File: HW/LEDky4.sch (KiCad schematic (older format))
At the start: 8 parts

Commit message: add some codes for JLCPCB, change package and schematic of CP2102
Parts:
- C? (x4): LCSC (none) -> C1525
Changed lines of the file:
@@
 F 2 "Capacitor_SMD:C_0402_1005Metric" H 2738 1450 50  0001 C CNN
 F 3 "~" H 2700 1600 50  0001 C CNN
+F 4 "C1525" H 2700 1600 50  0001 C CNN "LCSC"
 	1    2700 1600
 	1    0    0    -1
@@
 F 2 "Capacitor_SMD:C_0402_1005Metric" H 4138 1450 50  0001 C CNN
 F 3 "~" H 4100 1600 50  0001 C CNN
+F 4 "C1525" H 4100 1600 50  0001 C CNN "LCSC"
 	1    4100 1600
 	1    0    0    -1
@@
 F 2 "Capacitor_SMD:C_0402_1005Metric" H 5438 1450 50  0001 C CNN
 F 3 "~" H 5400 1600 50  0001 C CNN
+F 4 "C1525" H 5400 1600 50  0001 C CNN "LCSC"
 	1    5400 1600
 	1    0    0    -1
@@
 F 2 "Capacitor_SMD:C_0402_1005Metric" H 6838 1450 50  0001 C CNN
 F 3 "~" H 6800 1600 50  0001 C CNN
+F 4 "C1525" H 6800 1600 50  0001 C CNN "LCSC"
 	1    6800 1600
 	1    0    0    -1
@@
 F 2 "Capacitor_SMD:C_0402_1005Metric" H 2738 1450 50  0001 C CNN
 F 3 "~" H 2700 1600 50  0001 C CNN
+F 4 "C1525" H 2700 1600 50  0001 C CNN "LCSC"
 	1    2700 1600
 	1    0    0    -1
@@
 F 2 "Capacitor_SMD:C_0402_1005Metric" H 4138 1450 50  0001 C CNN
 F 3 "~" H 4100 1600 50  0001 C CNN
+F 4 "C1525" H 4100 1600 50  0001 C CNN "LCSC"
 	1    4100 1600
 	1    0    0    -1
@@
 F 2 "Capacitor_SMD:C_0402_1005Metric" H 5438 1450 50  0001 C CNN
 F 3 "~" H 5400 1600 50  0001 C CNN
+F 4 "C1525" H 5400 1600 50  0001 C CNN "LCSC"
 	1    5400 1600
 	1    0    0    -1
@@
 F 2 "Capacitor_SMD:C_0402_1005Metric" H 6838 1450 50  0001 C CNN
 F 3 "~" H 6800 1600 50  0001 C CNN
+F 4 "C1525" H 6800 1600 50  0001 C CNN "LCSC"
 	1    6800 1600
 	1    0    0    -1

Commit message: add some codes for JLCPCB
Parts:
- D? (x4): LCSC (none) -> C114587
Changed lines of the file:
@@
 F 2 "LED_SMD:LED_WS2812B_PLCC4_5.0x5.0mm_P3.2mm" H 2200 1500 50  0001 L TNN
 F 3 "https://cdn-shop.adafruit.com/datasheets/WS2812B.pdf" H 2250 1425 50  0001 L TNN
+F 4 "C114587" H 2150 1800 50  0001 C CNN "LCSC"
 	1    2150 1800
 	1    0    0    -1
@@
 F 2 "LED_SMD:LED_WS2812B_PLCC4_5.0x5.0mm_P3.2mm" H 3600 1500 50  0001 L TNN
 F 3 "https://cdn-shop.adafruit.com/datasheets/WS2812B.pdf" H 3650 1425 50  0001 L TNN
+F 4 "C114587" H 3550 1800 50  0001 C CNN "LCSC"
 	1    3550 1800
 	1    0    0    -1
@@
 F 2 "LED_SMD:LED_WS2812B_PLCC4_5.0x5.0mm_P3.2mm" H 4900 1500 50  0001 L TNN
 F 3 "https://cdn-shop.adafruit.com/datasheets/WS2812B.pdf" H 4950 1425 50  0001 L TNN
+F 4 "C114587" H 4850 1800 50  0001 C CNN "LCSC"
 	1    4850 1800
 	1    0    0    -1
@@
 F 2 "LED_SMD:LED_WS2812B_PLCC4_5.0x5.0mm_P3.2mm" H 6300 1500 50  0001 L TNN
 F 3 "https://cdn-shop.adafruit.com/datasheets/WS2812B.pdf" H 6350 1425 50  0001 L TNN
+F 4 "C114587" H 6250 1800 50  0001 C CNN "LCSC"
 	1    6250 1800
 	1    0    0    -1
@@
 F 2 "LED_SMD:LED_WS2812B_PLCC4_5.0x5.0mm_P3.2mm" H 2200 1500 50  0001 L TNN
 F 3 "https://cdn-shop.adafruit.com/datasheets/WS2812B.pdf" H 2250 1425 50  0001 L TNN
+F 4 "C114587" H 2150 1800 50  0001 C CNN "LCSC"
 	1    2150 1800
 	1    0    0    -1
@@
 F 2 "LED_SMD:LED_WS2812B_PLCC4_5.0x5.0mm_P3.2mm" H 3600 1500 50  0001 L TNN
 F 3 "https://cdn-shop.adafruit.com/datasheets/WS2812B.pdf" H 3650 1425 50  0001 L TNN
+F 4 "C114587" H 3550 1800 50  0001 C CNN "LCSC"
 	1    3550 1800
 	1    0    0    -1
@@
 F 2 "LED_SMD:LED_WS2812B_PLCC4_5.0x5.0mm_P3.2mm" H 4900 1500 50  0001 L TNN
 F 3 "https://cdn-shop.adafruit.com/datasheets/WS2812B.pdf" H 4950 1425 50  0001 L TNN
+F 4 "C114587" H 4850 1800 50  0001 C CNN "LCSC"
 	1    4850 1800
 	1    0    0    -1
@@
 F 2 "LED_SMD:LED_WS2812B_PLCC4_5.0x5.0mm_P3.2mm" H 6300 1500 50  0001 L TNN
 F 3 "https://cdn-shop.adafruit.com/datasheets/WS2812B.pdf" H 6350 1425 50  0001 L TNN
+F 4 "C114587" H 6250 1800 50  0001 C CNN "LCSC"
 	1    6250 1800
 	1    0    0    -1

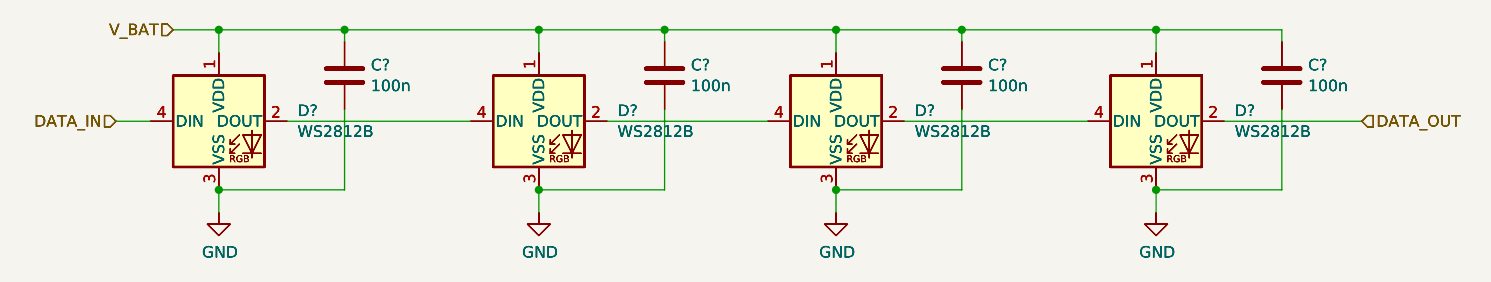
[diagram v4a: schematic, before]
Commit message: numbering components, place components on board
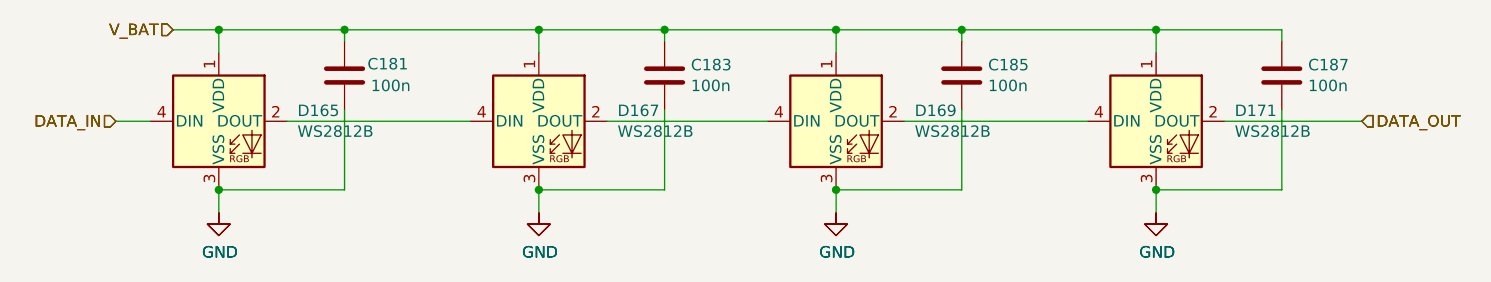
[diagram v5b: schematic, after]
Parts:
- removed C? (x4): 100n, Capacitor_SMD:C_0402_1005Metric, symbol Device:C
- removed D? (x4): WS2812B, LED_SMD:LED_WS2812B_PLCC4_5.0x5.0mm_P3.2mm, symbol LED:WS2812B
- added C117, C119, C121, C123: 100n, Capacitor_SMD:C_0402_1005Metric, symbol Device:C
- added D101, D103, D105, D107: WS2812B, LED_SMD:LED_WS2812B_PLCC4_5.0x5.0mm_P3.2mm, symbol LED:WS2812B
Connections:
- net DATA_IN: now also D101.4 (DIN)
- net DATA_OUT: now also D107.2 (DOUT)
- net GND: now also C117.2, C119.2, C121.2, C123.2, D101.3 (VSS), D103.3 (VSS), D105.3 (VSS), D107.3 (VSS)
- net V_BAT: now also C117.1, C119.1, C121.1, C123.1, D101.1 (VDD), D103.1 (VDD), D105.1 (VDD), D107.1 (VDD)
- new net: D101.2 (DOUT), D103.4 (DIN)
- new net: D103.2 (DOUT), D105.4 (DIN)
- new net: D105.2 (DOUT), D107.4 (DIN)

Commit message: repair package of TP4056
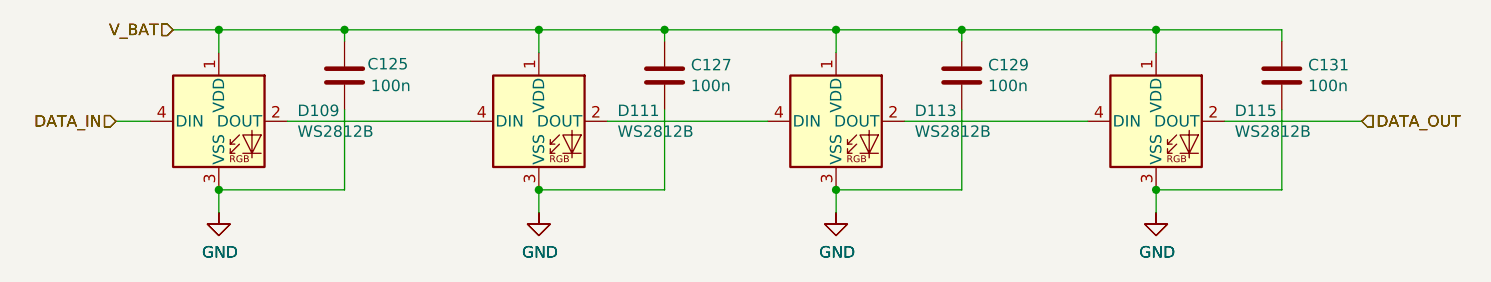
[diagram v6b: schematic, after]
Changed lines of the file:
@@
 $Descr A4 11693 8268
 encoding utf-8
-Sheet 42 44
+Sheet 35 44
 Title ""
 Date ""
@@
 AR Path="/5F79BCD0/5F79846B/5F78FD5C" Ref="#PWR0218"  Part="1"
 AR Path="/5F79BCD0/5F798482/5F78FD5C" Ref="#PWR0226"  Part="1"
-F 0 "#PWR0306" H 2150 1950 50  0001 C CNN
+F 0 "#PWR0250" H 2150 1950 50  0001 C CNN
 F 1 "GND" H 2155 2027 50  0000 C CNN
 F 2 "" H 2150 2200 50  0001 C CNN
@@
 AR Path="/5F79BCD0/5F79846B/5F78FD62" Ref="C93"  Part="1"
 AR Path="/5F79BCD0/5F798482/5F78FD62" Ref="C101"  Part="1"
-F 0 "C181" H 2800 1650 50  0000 L CNN
+F 0 "C125" H 2800 1650 50  0000 L CNN
 F 1 "100n" H 2815 1555 50  0000 L CNN
 F 2 "Capacitor_SMD:C_0402_1005Metric" H 2738 1450 50  0001 C CNN
@@
 AR Path="/5F79BCD0/5F79846B/5F78FD71" Ref="D79"  Part="1"
 AR Path="/5F79BCD0/5F798482/5F78FD71" Ref="D87"  Part="1"
-F 0 "D167" H 3894 1846 50  0000 L CNN
+F 0 "D111" H 3894 1846 50  0000 L CNN
 F 1 "WS2812B" H 3894 1755 50  0000 L CNN
 F 2 "LED_SMD:LED_WS2812B_PLCC4_5.0x5.0mm_P3.2mm" H 3600 1500 50  0001 L TNN
@@
 AR Path="/5F79BCD0/5F79846B/5F798BEB" Ref="#PWR0219"  Part="1"
 AR Path="/5F79BCD0/5F798482/5F798BEB" Ref="#PWR0227"  Part="1"
-F 0 "#PWR0307" H 3550 1950 50  0001 C CNN
+F 0 "#PWR0251" H 3550 1950 50  0001 C CNN
 F 1 "GND" H 3555 2027 50  0000 C CNN
 F 2 "" H 3550 2200 50  0001 C CNN
@@
 AR Path="/5F79BCD0/5F79846B/5F798BEE" Ref="#PWR0220"  Part="1"
 AR Path="/5F79BCD0/5F798482/5F798BEE" Ref="#PWR0228"  Part="1"
-F 0 "#PWR0308" H 4850 1950 50  0001 C CNN
+F 0 "#PWR0252" H 4850 1950 50  0001 C CNN
 F 1 "GND" H 4855 2027 50  0000 C CNN
 F 2 "" H 4850 2200 50  0001 C CNN
@@
 AR Path="/5F79BCD0/5F79846B/5F78FDA5" Ref="D83"  Part="1"
 AR Path="/5F79BCD0/5F798482/5F78FDA5" Ref="D91"  Part="1"
-F 0 "D171" H 6594 1846 50  0000 L CNN
+F 0 "D115" H 6594 1846 50  0000 L CNN
 F 1 "WS2812B" H 6594 1755 50  0000 L CNN
 F 2 "LED_SMD:LED_WS2812B_PLCC4_5.0x5.0mm_P3.2mm" H 6300 1500 50  0001 L TNN
@@
 AR Path="/5F79BCD0/5F79846B/5F78FDAB" Ref="#PWR0221"  Part="1"
 AR Path="/5F79BCD0/5F798482/5F78FDAB" Ref="#PWR0229"  Part="1"
-F 0 "#PWR0309" H 6250 1950 50  0001 C CNN
+F 0 "#PWR0253" H 6250 1950 50  0001 C CNN
 F 1 "GND" H 6255 2027 50  0000 C CNN
 F 2 "" H 6250 2200 50  0001 C CNN
@@
 AR Path="/5F79BCD0/5F79846B/5F78FDB1" Ref="C99"  Part="1"
 AR Path="/5F79BCD0/5F798482/5F78FDB1" Ref="C107"  Part="1"
-F 0 "C187" H 6915 1646 50  0000 L CNN
+F 0 "C131" H 6915 1646 50  0000 L CNN
 F 1 "100n" H 6915 1555 50  0000 L CNN
 F 2 "Capacitor_SMD:C_0402_1005Metric" H 6838 1450 50  0001 C CNN
@@
 AR Path="/5F79BCD0/5F79846B/5F78FD56" Ref="D77"  Part="1"
 AR Path="/5F79BCD0/5F798482/5F78FD56" Ref="D85"  Part="1"
-F 0 "D165" H 2494 1846 50  0000 L CNN
+F 0 "D109" H 2494 1846 50  0000 L CNN
 F 1 "WS2812B" H 2494 1755 50  0000 L CNN
 F 2 "LED_SMD:LED_WS2812B_PLCC4_5.0x5.0mm_P3.2mm" H 2200 1500 50  0001 L TNN
@@
 AR Path="/5F79BCD0/5F79846B/5F798BE8" Ref="#PWR0222"  Part="1"
 AR Path="/5F79BCD0/5F798482/5F798BE8" Ref="#PWR0230"  Part="1"
-F 0 "#PWR0310" H 2150 1950 50  0001 C CNN
+F 0 "#PWR0254" H 2150 1950 50  0001 C CNN
 F 1 "GND" H 2155 2027 50  0000 C CNN
 F 2 "" H 2150 2200 50  0001 C CNN
@@
 AR Path="/5F79BCD0/5F79846B/5F78FD77" Ref="#PWR0223"  Part="1"
 AR Path="/5F79BCD0/5F798482/5F78FD77" Ref="#PWR0231"  Part="1"
-F 0 "#PWR0311" H 3550 1950 50  0001 C CNN
+F 0 "#PWR0255" H 3550 1950 50  0001 C CNN
 F 1 "GND" H 3555 2027 50  0000 C CNN
 F 2 "" H 3550 2200 50  0001 C CNN
@@
 AR Path="/5F79BCD0/5F79846B/5F78FD7D" Ref="C95"  Part="1"
 AR Path="/5F79BCD0/5F798482/5F78FD7D" Ref="C103"  Part="1"
-F 0 "C183" H 4215 1646 50  0000 L CNN
+F 0 "C127" H 4215 1646 50  0000 L CNN
 F 1 "100n" H 4215 1555 50  0000 L CNN
 F 2 "Capacitor_SMD:C_0402_1005Metric" H 4138 1450 50  0001 C CNN
@@
 AR Path="/5F79BCD0/5F79846B/5F78FD8B" Ref="D81"  Part="1"
 AR Path="/5F79BCD0/5F798482/5F78FD8B" Ref="D89"  Part="1"
-F 0 "D169" H 5194 1846 50  0000 L CNN
+F 0 "D113" H 5194 1846 50  0000 L CNN
 F 1 "WS2812B" H 5194 1755 50  0000 L CNN
 F 2 "LED_SMD:LED_WS2812B_PLCC4_5.0x5.0mm_P3.2mm" H 4900 1500 50  0001 L TNN
@@
 AR Path="/5F79BCD0/5F79846B/5F78FD91" Ref="#PWR0224"  Part="1"
 AR Path="/5F79BCD0/5F798482/5F78FD91" Ref="#PWR0232"  Part="1"
-F 0 "#PWR0312" H 4850 1950 50  0001 C CNN
+F 0 "#PWR0256" H 4850 1950 50  0001 C CNN
 F 1 "GND" H 4855 2027 50  0000 C CNN
 F 2 "" H 4850 2200 50  0001 C CNN
@@
 AR Path="/5F79BCD0/5F79846B/5F78FD97" Ref="C97"  Part="1"
 AR Path="/5F79BCD0/5F798482/5F78FD97" Ref="C105"  Part="1"
-F 0 "C185" H 5515 1646 50  0000 L CNN
+F 0 "C129" H 5515 1646 50  0000 L CNN
 F 1 "100n" H 5515 1555 50  0000 L CNN
 F 2 "Capacitor_SMD:C_0402_1005Metric" H 5438 1450 50  0001 C CNN
@@
 AR Path="/5F79BCD0/5F79846B/5F798BF1" Ref="#PWR0225"  Part="1"
 AR Path="/5F79BCD0/5F798482/5F798BF1" Ref="#PWR0233"  Part="1"
-F 0 "#PWR0313" H 6250 1950 50  0001 C CNN
+F 0 "#PWR0257" H 6250 1950 50  0001 C CNN
 F 1 "GND" H 6255 2027 50  0000 C CNN
 F 2 "" H 6250 2200 50  0001 C CNN

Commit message: repair mistake with buttons
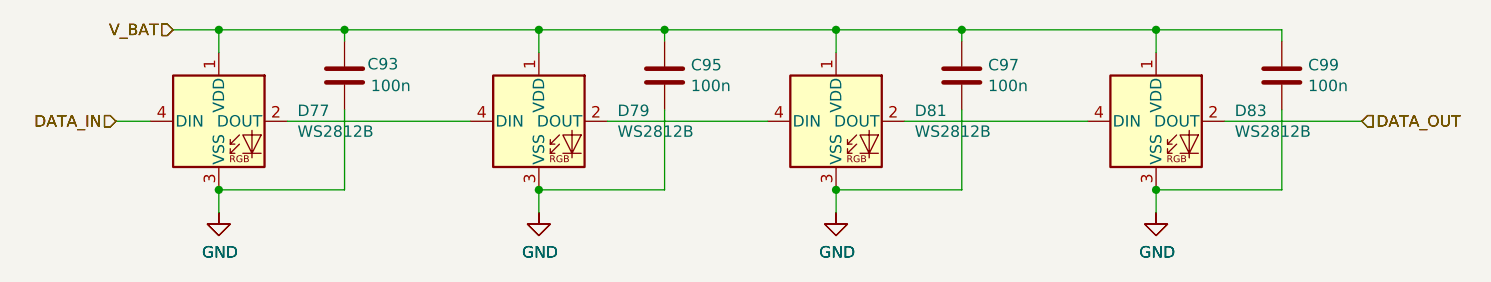
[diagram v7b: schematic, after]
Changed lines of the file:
@@
 $Descr A4 11693 8268
 encoding utf-8
-Sheet 35 44
+Sheet 30 44
 Title ""
 Date ""
@@
 AR Path="/5F79BCD0/5F79846B/5F78FD5C" Ref="#PWR0218"  Part="1"
 AR Path="/5F79BCD0/5F798482/5F78FD5C" Ref="#PWR0226"  Part="1"
-F 0 "#PWR0250" H 2150 1950 50  0001 C CNN
+F 0 "#PWR0306" H 2150 1950 50  0001 C CNN
 F 1 "GND" H 2155 2027 50  0000 C CNN
 F 2 "" H 2150 2200 50  0001 C CNN
@@
 AR Path="/5F79BCD0/5F79846B/5F78FD62" Ref="C93"  Part="1"
 AR Path="/5F79BCD0/5F798482/5F78FD62" Ref="C101"  Part="1"
-F 0 "C125" H 2800 1650 50  0000 L CNN
+F 0 "C93" H 2800 1650 50  0000 L CNN
 F 1 "100n" H 2815 1555 50  0000 L CNN
 F 2 "Capacitor_SMD:C_0402_1005Metric" H 2738 1450 50  0001 C CNN
@@
 AR Path="/5F79BCD0/5F79846B/5F78FD71" Ref="D79"  Part="1"
 AR Path="/5F79BCD0/5F798482/5F78FD71" Ref="D87"  Part="1"
-F 0 "D111" H 3894 1846 50  0000 L CNN
+F 0 "D79" H 3894 1846 50  0000 L CNN
 F 1 "WS2812B" H 3894 1755 50  0000 L CNN
 F 2 "LED_SMD:LED_WS2812B_PLCC4_5.0x5.0mm_P3.2mm" H 3600 1500 50  0001 L TNN
@@
 AR Path="/5F79BCD0/5F79846B/5F798BEB" Ref="#PWR0219"  Part="1"
 AR Path="/5F79BCD0/5F798482/5F798BEB" Ref="#PWR0227"  Part="1"
-F 0 "#PWR0251" H 3550 1950 50  0001 C CNN
+F 0 "#PWR0307" H 3550 1950 50  0001 C CNN
 F 1 "GND" H 3555 2027 50  0000 C CNN
 F 2 "" H 3550 2200 50  0001 C CNN
@@
 AR Path="/5F79BCD0/5F79846B/5F798BEE" Ref="#PWR0220"  Part="1"
 AR Path="/5F79BCD0/5F798482/5F798BEE" Ref="#PWR0228"  Part="1"
-F 0 "#PWR0252" H 4850 1950 50  0001 C CNN
+F 0 "#PWR0308" H 4850 1950 50  0001 C CNN
 F 1 "GND" H 4855 2027 50  0000 C CNN
 F 2 "" H 4850 2200 50  0001 C CNN
@@
 AR Path="/5F79BCD0/5F79846B/5F78FDA5" Ref="D83"  Part="1"
 AR Path="/5F79BCD0/5F798482/5F78FDA5" Ref="D91"  Part="1"
-F 0 "D115" H 6594 1846 50  0000 L CNN
+F 0 "D83" H 6594 1846 50  0000 L CNN
 F 1 "WS2812B" H 6594 1755 50  0000 L CNN
 F 2 "LED_SMD:LED_WS2812B_PLCC4_5.0x5.0mm_P3.2mm" H 6300 1500 50  0001 L TNN
@@
 AR Path="/5F79BCD0/5F79846B/5F78FDAB" Ref="#PWR0221"  Part="1"
 AR Path="/5F79BCD0/5F798482/5F78FDAB" Ref="#PWR0229"  Part="1"
-F 0 "#PWR0253" H 6250 1950 50  0001 C CNN
+F 0 "#PWR0309" H 6250 1950 50  0001 C CNN
 F 1 "GND" H 6255 2027 50  0000 C CNN
 F 2 "" H 6250 2200 50  0001 C CNN
@@
 AR Path="/5F79BCD0/5F79846B/5F78FDB1" Ref="C99"  Part="1"
 AR Path="/5F79BCD0/5F798482/5F78FDB1" Ref="C107"  Part="1"
-F 0 "C131" H 6915 1646 50  0000 L CNN
+F 0 "C99" H 6915 1646 50  0000 L CNN
 F 1 "100n" H 6915 1555 50  0000 L CNN
 F 2 "Capacitor_SMD:C_0402_1005Metric" H 6838 1450 50  0001 C CNN
@@
 AR Path="/5F79BCD0/5F79846B/5F78FD56" Ref="D77"  Part="1"
 AR Path="/5F79BCD0/5F798482/5F78FD56" Ref="D85"  Part="1"
-F 0 "D109" H 2494 1846 50  0000 L CNN
+F 0 "D77" H 2494 1846 50  0000 L CNN
 F 1 "WS2812B" H 2494 1755 50  0000 L CNN
 F 2 "LED_SMD:LED_WS2812B_PLCC4_5.0x5.0mm_P3.2mm" H 2200 1500 50  0001 L TNN
@@
 AR Path="/5F79BCD0/5F79846B/5F798BE8" Ref="#PWR0222"  Part="1"
 AR Path="/5F79BCD0/5F798482/5F798BE8" Ref="#PWR0230"  Part="1"
-F 0 "#PWR0254" H 2150 1950 50  0001 C CNN
+F 0 "#PWR0310" H 2150 1950 50  0001 C CNN
 F 1 "GND" H 2155 2027 50  0000 C CNN
 F 2 "" H 2150 2200 50  0001 C CNN
@@
 AR Path="/5F79BCD0/5F79846B/5F78FD77" Ref="#PWR0223"  Part="1"
 AR Path="/5F79BCD0/5F798482/5F78FD77" Ref="#PWR0231"  Part="1"
-F 0 "#PWR0255" H 3550 1950 50  0001 C CNN
+F 0 "#PWR0311" H 3550 1950 50  0001 C CNN
 F 1 "GND" H 3555 2027 50  0000 C CNN
 F 2 "" H 3550 2200 50  0001 C CNN
@@
 AR Path="/5F79BCD0/5F79846B/5F78FD7D" Ref="C95"  Part="1"
 AR Path="/5F79BCD0/5F798482/5F78FD7D" Ref="C103"  Part="1"
-F 0 "C127" H 4215 1646 50  0000 L CNN
+F 0 "C95" H 4215 1646 50  0000 L CNN
 F 1 "100n" H 4215 1555 50  0000 L CNN
 F 2 "Capacitor_SMD:C_0402_1005Metric" H 4138 1450 50  0001 C CNN
@@
 AR Path="/5F79BCD0/5F79846B/5F78FD8B" Ref="D81"  Part="1"
 AR Path="/5F79BCD0/5F798482/5F78FD8B" Ref="D89"  Part="1"
-F 0 "D113" H 5194 1846 50  0000 L CNN
+F 0 "D81" H 5194 1846 50  0000 L CNN
 F 1 "WS2812B" H 5194 1755 50  0000 L CNN
 F 2 "LED_SMD:LED_WS2812B_PLCC4_5.0x5.0mm_P3.2mm" H 4900 1500 50  0001 L TNN
@@
 AR Path="/5F79BCD0/5F79846B/5F78FD91" Ref="#PWR0224"  Part="1"
 AR Path="/5F79BCD0/5F798482/5F78FD91" Ref="#PWR0232"  Part="1"
-F 0 "#PWR0256" H 4850 1950 50  0001 C CNN
+F 0 "#PWR0312" H 4850 1950 50  0001 C CNN
 F 1 "GND" H 4855 2027 50  0000 C CNN
 F 2 "" H 4850 2200 50  0001 C CNN
@@
 AR Path="/5F79BCD0/5F79846B/5F78FD97" Ref="C97"  Part="1"
 AR Path="/5F79BCD0/5F798482/5F78FD97" Ref="C105"  Part="1"
-F 0 "C129" H 5515 1646 50  0000 L CNN
+F 0 "C97" H 5515 1646 50  0000 L CNN
 F 1 "100n" H 5515 1555 50  0000 L CNN
 F 2 "Capacitor_SMD:C_0402_1005Metric" H 5438 1450 50  0001 C CNN
@@
 AR Path="/5F79BCD0/5F79846B/5F798BF1" Ref="#PWR0225"  Part="1"
 AR Path="/5F79BCD0/5F798482/5F798BF1" Ref="#PWR0233"  Part="1"
-F 0 "#PWR0257" H 6250 1950 50  0001 C CNN
+F 0 "#PWR0313" H 6250 1950 50  0001 C CNN
 F 1 "GND" H 6255 2027 50  0000 C CNN
 F 2 "" H 6250 2200 50  0001 C CNN
